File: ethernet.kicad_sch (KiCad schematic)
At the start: 62 parts, among them J6 Bus_RJ45_6-2337992-8, U15 KSZ9031RNXCA, Y2 Resonator_25MHz_ABM8G

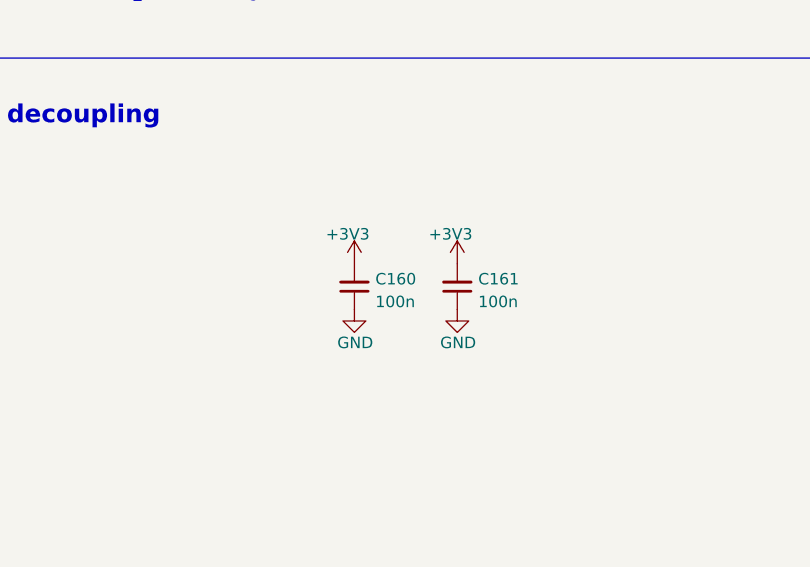
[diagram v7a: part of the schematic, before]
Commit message: [#68199] Start implementing changes after the PCB review
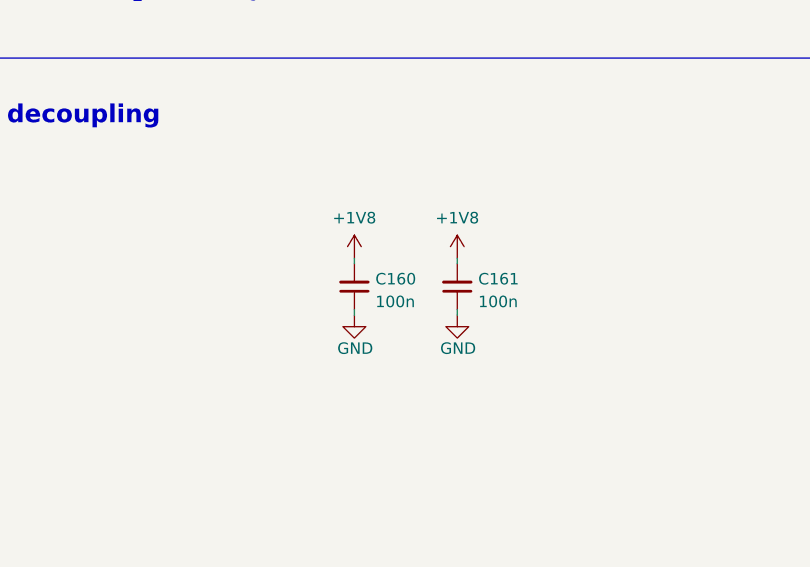
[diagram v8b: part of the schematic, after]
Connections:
- net +1V8: now also C160.2, C161.2
- net +3V3: no longer C160.2, C161.2
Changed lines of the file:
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@@
     (stroke (width 0) (type default))
   )
+  (wire (pts (xy 339.09 231.775) (xy 339.09 232.41))
+    (stroke (width 0) (type default))
+  )
   (wire (pts (xy 153.67 168.91) (xy 166.37 168.91))
     (stroke (width 0) (type default))
@@
     (stroke (width 0) (type default))
   )
+  (wire (pts (xy 327.66 238.125) (xy 327.66 237.49))
+    (stroke (width 0) (type default))
+  )
   (wire (pts (xy 360.68 66.04) (xy 360.68 68.58))
     (stroke (width 0) (type default))
@@
     (stroke (width 0) (type default))
   )
+  (wire (pts (xy 339.09 238.125) (xy 339.09 237.49))
+    (stroke (width 0) (type default))
+  )
   (wire (pts (xy 175.26 105.41) (xy 175.26 107.95))
     (stroke (width 0) (type default))
@@
     (stroke (width 0) (type default))
   )
+  (wire (pts (xy 327.66 231.775) (xy 327.66 232.41))
+    (stroke (width 0) (type default))
+  )
   (wire (pts (xy 372.11 171.45) (xy 372.11 173.99))
     (stroke (width 0) (type default))
@@
     )
   )
+  (symbol (lib_id "antmicropower:+1V8") (at 339.09 231.775 0) (unit 1)
+    (in_bom yes) (on_board yes) (dnp no) (fields_autoplaced)
+    (property "Reference" "#PWR0254" (at 354.33 234.315 0)
+      (effects (font (size 1.27 1.27) (thickness 0.15)) (justify left bottom) hide)
+    )
+    (property "Value" "+1V8" (at 339.09 227.33 0)
+      (effects (font (size 1.27 1.27) (thickness 0.15)))
+    )
+    (property "Footprint" "" (at 354.33 239.395 0)
+      (effects (font (size 1.27 1.27) (thickness 0.15)) (justify left bottom) hide)
+    )
+    (property "Datasheet" "" (at 354.33 241.935 0)
+      (effects (font (size 1.27 1.27) (thickness 0.15)) (justify left bottom) hide)
+    )
+    (property "Author" "Antmicro" (at 354.33 236.855 0)
+      (effects (font (size 1.27 1.27) (thickness 0.15)) (justify left bottom) hide)
+    )
+    (property "License" "Apache-2.0" (at 354.33 239.395 0)
+      (effects (font (size 1.27 1.27) (thickness 0.15)) (justify left bottom) hide)
+    )
+    (pin "1")
+    (instances
+      (project "data-center-rdimm-ddr5-tester"
+        (path "/1faa6543-e26a-4449-8bac-ee14b9f19e5f/00000000-0000-0000-0000-00005f982999"
+          (reference "#PWR0254") (unit 1)
+        )
+      )
+    )
+  )
+  (symbol (lib_id "antmicropower:+1V8") (at 327.66 231.775 0) (unit 1)
+    (in_bom yes) (on_board yes) (dnp no) (fields_autoplaced)
+    (property "Reference" "#PWR0252" (at 342.9 234.315 0)
+      (effects (font (size 1.27 1.27) (thickness 0.15)) (justify left bottom) hide)
+    )
+    (property "Value" "+1V8" (at 327.66 227.33 0)
+      (effects (font (size 1.27 1.27) (thickness 0.15)))
+    )
+    (property "Footprint" "" (at 342.9 239.395 0)
+      (effects (font (size 1.27 1.27) (thickness 0.15)) (justify left bottom) hide)
+    )
+    (property "Datasheet" "" (at 342.9 241.935 0)
+      (effects (font (size 1.27 1.27) (thickness 0.15)) (justify left bottom) hide)
+    )
+    (property "Author" "Antmicro" (at 342.9 236.855 0)
+      (effects (font (size 1.27 1.27) (thickness 0.15)) (justify left bottom) hide)
+    )
+    (property "License" "Apache-2.0" (at 342.9 239.395 0)
+      (effects (font (size 1.27 1.27) (thickness 0.15)) (justify left bottom) hide)
+    )
+    (pin "1")
+    (instances
+      (project "data-center-rdimm-ddr5-tester"
+        (path "/1faa6543-e26a-4449-8bac-ee14b9f19e5f/00000000-0000-0000-0000-00005f982999"
+          (reference "#PWR0252") (unit 1)
+        )
+      )
+    )
+  )
   (symbol (lib_id "antmicropower:GND") (at 182.88 114.3 0) (mirror y) (unit 1)
     (in_bom yes) (on_board yes) (dnp no) (fields_autoplaced)
@@
     )
   )
-  (symbol (lib_id "antmicropower:GND") (at 327.66 237.49 0) (unit 1)
+  (symbol (lib_id "antmicropower:GND") (at 327.66 238.125 0) (unit 1)
     (in_bom yes) (on_board yes) (dnp no) (fields_autoplaced)
-    (property "Reference" "#PWR0253" (at 327.66 243.84 0)
+    (property "Reference" "#PWR0253" (at 327.66 244.475 0)
       (effects (font (size 1.27 1.27)) hide)
     )
-    (property "Value" "GND" (at 325.755 241.935 0)
+    (property "Value" "GND" (at 325.755 242.57 0)
       (effects (font (size 1.27 1.27) (thickness 0.15)) (justify left bottom))
     )
-    (property "Footprint" "" (at 336.55 245.11 0)
+    (property "Footprint" "" (at 336.55 245.745 0)
       (effects (font (size 1.27 1.27) (thickness 0.15)) (justify left bottom) hide)
     )
-    (property "Datasheet" "" (at 336.55 250.19 0)
+    (property "Datasheet" "" (at 336.55 250.825 0)
       (effects (font (size 1.27 1.27) (thickness 0.15)) (justify left bottom) hide)
     )
-    (property "Author" "Antmicro" (at 336.55 242.57 0)
+    (property "Author" "Antmicro" (at 336.55 243.205 0)
       (effects (font (size 1.27 1.27) (thickness 0.15)) (justify left bottom) hide)
     )
-    (property "License" "Apache-2.0" (at 336.55 245.11 0)
+    (property "License" "Apache-2.0" (at 336.55 245.745 0)
       (effects (font (size 1.27 1.27) (thickness 0.15)) (justify left bottom) hide)
     )
@@
     )
   )
-  (symbol (lib_id "antmicropower:+3V3") (at 339.09 232.41 0) (unit 1)
-    (in_bom yes) (on_board yes) (dnp no)
-    (property "Reference" "#PWR0254" (at 339.09 236.22 0)
-      (effects (font (size 1.27 1.27)) hide)
-    )
-    (property "Value" "+3V3" (at 335.915 229.87 0)
-      (effects (font (size 1.27 1.27) (thickness 0.15)) (justify left bottom))
-    )
-    (property "Footprint" "" (at 354.33 240.03 0)
-      (effects (font (size 1.27 1.27) (thickness 0.15)) (justify left bottom) hide)
-    )
-    (property "Datasheet" "" (at 354.33 242.57 0)
-      (effects (font (size 1.27 1.27) (thickness 0.15)) (justify left bottom) hide)
-    )
-    (property "Author" "Antmicro" (at 354.33 234.95 0)
-      (effects (font (size 1.27 1.27) (thickness 0.15)) (justify left bottom) hide)
-    )
-    (property "License" "Apache-2.0" (at 354.33 237.49 0)
-      (effects (font (size 1.27 1.27) (thickness 0.15)) (justify left bottom) hide)
-    )
-    (pin "1")
-    (instances
-      (project "data-center-rdimm-ddr5-tester"
-        (path "/1faa6543-e26a-4449-8bac-ee14b9f19e5f/00000000-0000-0000-0000-00005f982999"
-          (reference "#PWR0254") (unit 1)
-        )
-      )
-    )
-  )
   (symbol (lib_id "antmicropower:GND") (at 60.96 113.03 0) (unit 1)
     (in_bom yes) (on_board yes) (dnp no)
@@
     )
   )
-  (symbol (lib_id "antmicropower:+3V3") (at 327.66 232.41 0) (unit 1)
-    (in_bom yes) (on_board yes) (dnp no)
-    (property "Reference" "#PWR0252" (at 327.66 236.22 0)
-      (effects (font (size 1.27 1.27)) hide)
-    )
-    (property "Value" "+3V3" (at 324.485 229.87 0)
-      (effects (font (size 1.27 1.27) (thickness 0.15)) (justify left bottom))
-    )
-    (property "Footprint" "" (at 342.9 240.03 0)
-      (effects (font (size 1.27 1.27) (thickness 0.15)) (justify left bottom) hide)
-    )
-    (property "Datasheet" "" (at 342.9 242.57 0)
-      (effects (font (size 1.27 1.27) (thickness 0.15)) (justify left bottom) hide)
-    )
-    (property "Author" "Antmicro" (at 342.9 234.95 0)
-      (effects (font (size 1.27 1.27) (thickness 0.15)) (justify left bottom) hide)
-    )
-    (property "License" "Apache-2.0" (at 342.9 237.49 0)
-      (effects (font (size 1.27 1.27) (thickness 0.15)) (justify left bottom) hide)
-    )
-    (pin "1")
-    (instances
-      (project "data-center-rdimm-ddr5-tester"
-        (path "/1faa6543-e26a-4449-8bac-ee14b9f19e5f/00000000-0000-0000-0000-00005f982999"
-          (reference "#PWR0252") (unit 1)
-        )
-      )
-    )
-  )
   (symbol (lib_id "antmicroResistors0402:R_10k_0402") (at 317.5 171.45 0) (mirror y) (unit 1)
     (in_bom no) (on_board yes) (dnp yes)
@@
     )
   )
-  (symbol (lib_id "antmicropower:GND") (at 339.09 237.49 0) (unit 1)
+  (symbol (lib_id "antmicropower:GND") (at 339.09 238.125 0) (unit 1)
     (in_bom yes) (on_board yes) (dnp no) (fields_autoplaced)
-    (property "Reference" "#PWR0255" (at 339.09 243.84 0)
+    (property "Reference" "#PWR0255" (at 339.09 244.475 0)
       (effects (font (size 1.27 1.27)) hide)
     )
-    (property "Value" "GND" (at 337.185 241.935 0)
+    (property "Value" "GND" (at 337.185 242.57 0)
       (effects (font (size 1.27 1.27) (thickness 0.15)) (justify left bottom))
     )
-    (property "Footprint" "" (at 347.98 245.11 0)
+    (property "Footprint" "" (at 347.98 245.745 0)
       (effects (font (size 1.27 1.27) (thickness 0.15)) (justify left bottom) hide)
     )
-    (property "Datasheet" "" (at 347.98 250.19 0)
+    (property "Datasheet" "" (at 347.98 250.825 0)
       (effects (font (size 1.27 1.27) (thickness 0.15)) (justify left bottom) hide)
     )
-    (property "Author" "Antmicro" (at 347.98 242.57 0)
+    (property "Author" "Antmicro" (at 347.98 243.205 0)
       (effects (font (size 1.27 1.27) (thickness 0.15)) (justify left bottom) hide)
     )
-    (property "License" "Apache-2.0" (at 347.98 245.11 0)
+    (property "License" "Apache-2.0" (at 347.98 245.745 0)
       (effects (font (size 1.27 1.27) (thickness 0.15)) (justify left bottom) hide)
     )
